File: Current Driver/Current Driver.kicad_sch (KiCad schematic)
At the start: 58 parts, among them J1 Conn_01x03, J2 Input, J3 Load, J4 VP BJT Conn, J5 VN BJT Conn, Q1 BC817, Q2 BC807, Q3 D45H11G, Q4 D44H11G, Q5 D45H11, Q6 D44H11G, U1 ADA4622-2xCP, U2 ADA4622-2xCP

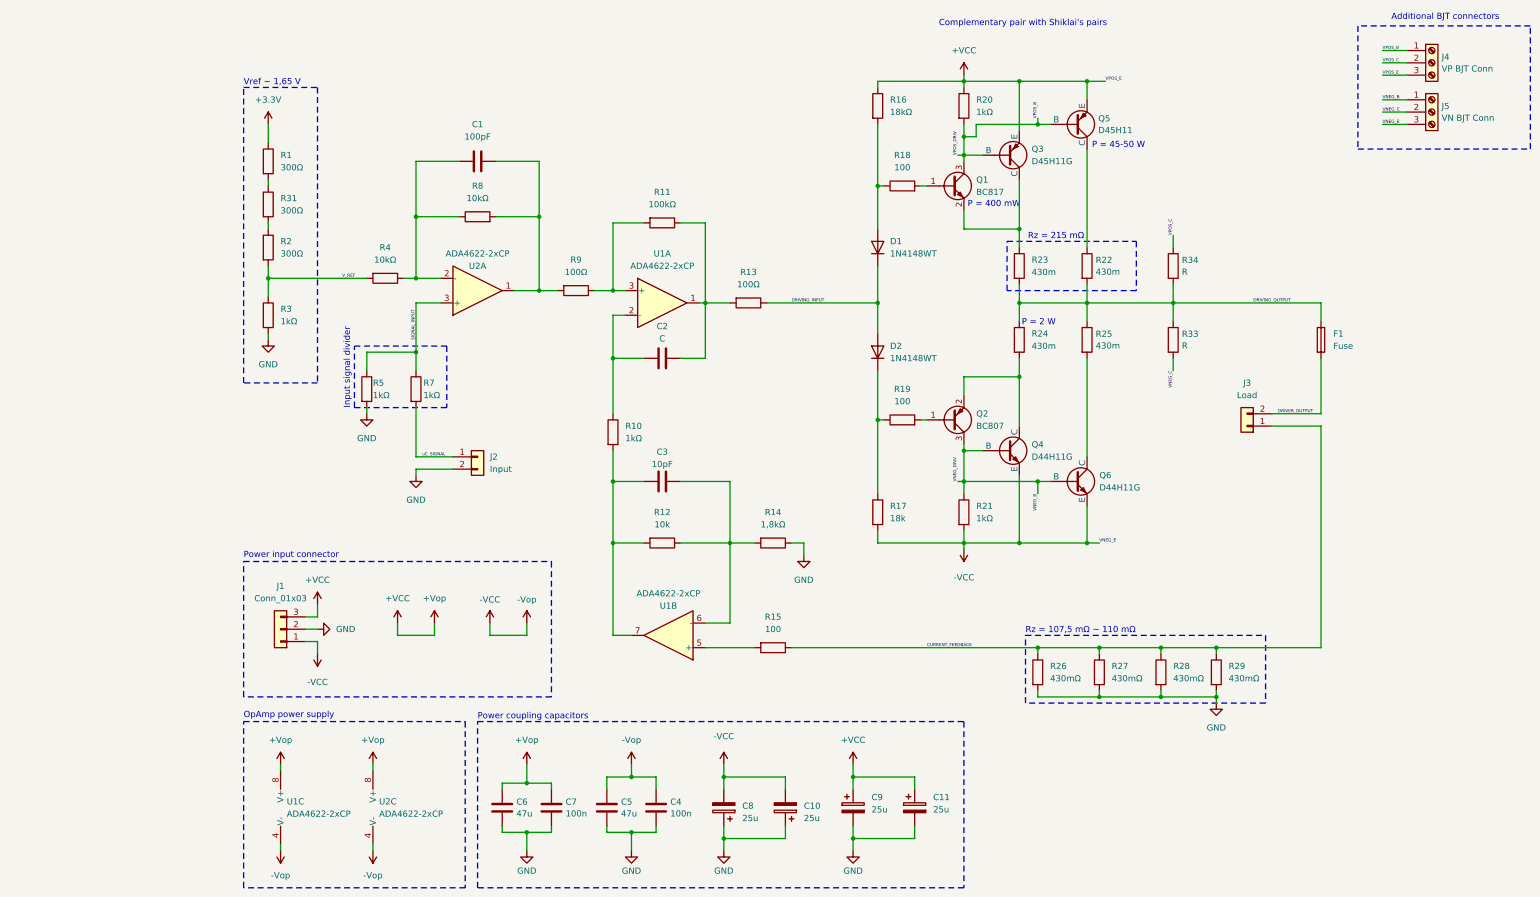
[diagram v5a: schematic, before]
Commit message: Edit Schematic
Added opAmp for stable reference voltage. Anotated schematic
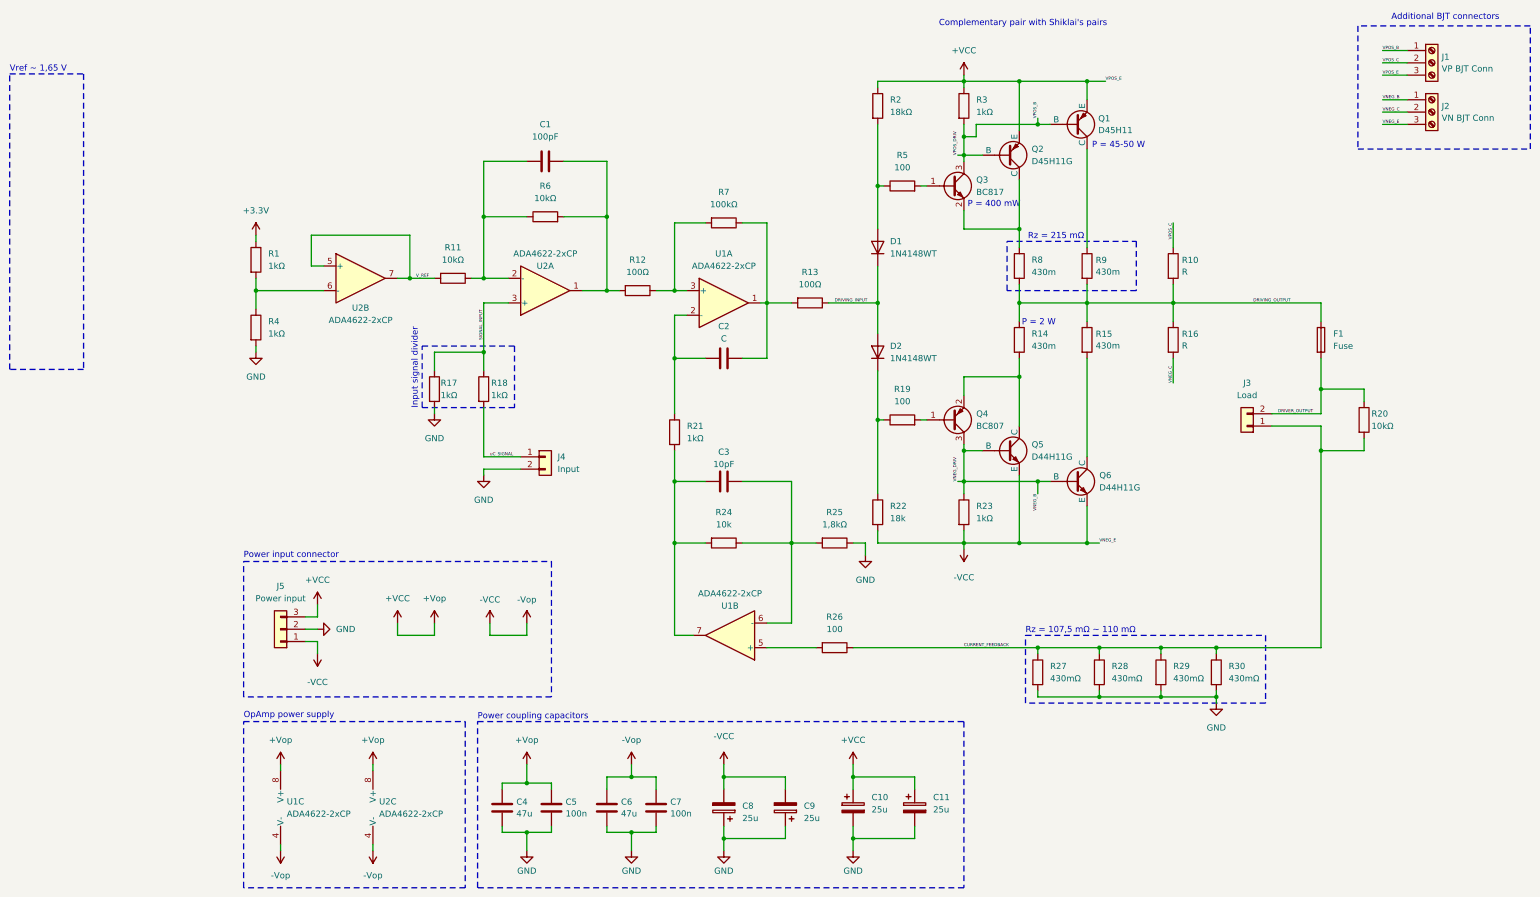
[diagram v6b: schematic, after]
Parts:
- removed R1, R31: 300Ω, Resistor_SMD:R_0805_2012Metric_Pad1.20x1.40mm_HandSolder, symbol Device:R
- added R20: 10kΩ, Resistor_SMD:R_0805_2012Metric_Pad1.20x1.40mm_HandSolder, symbol Device:R
- added unit 2 of U2
- J5: renamed from J1; value Conn_01x03 -> Power input
- R1: renamed from R2; value 300Ω -> 1kΩ
- renumbered C9 to C10, C6 to C4, C7 to C5, C5 to C6, C4 to C7, C10 to C9, J4 to J1, J5 to J2, J2 to J4, Q5 to Q1, Q3 to Q2, Q1 to Q3, Q2 to Q4, Q4 to Q5, R34 to R10, R4 to R11, R9 to R12, R24 to R14, R25 to R15, R33 to R16, R5 to R17, R7 to R18, R16 to R2, R10 to R21, R17 to R22, R21 to R23, R12 to R24, R14 to R25, R15 to R26, R26 to R27, R27 to R28, R28 to R29, R20 to R3, R29 to R30, R3 to R4, R18 to R5, R8 to R6, R11 to R7, R23 to R8, R22 to R9
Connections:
- net +3.3V: now also R1.1
- net CURRENT_FEEDBACK: now also R20.2
- net DRIVER_OUTPUT: now also R20.1
- net V_REF: now also U2.5 (+), U2.7; no longer R1.2, R4.1
- new net: R1.2, R4.1, U2.6 (-)
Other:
- moved on the sheet: C1, C2, C3, J4, R1, R11, R12, R13, R17, R18, R21, R24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

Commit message: schematic update
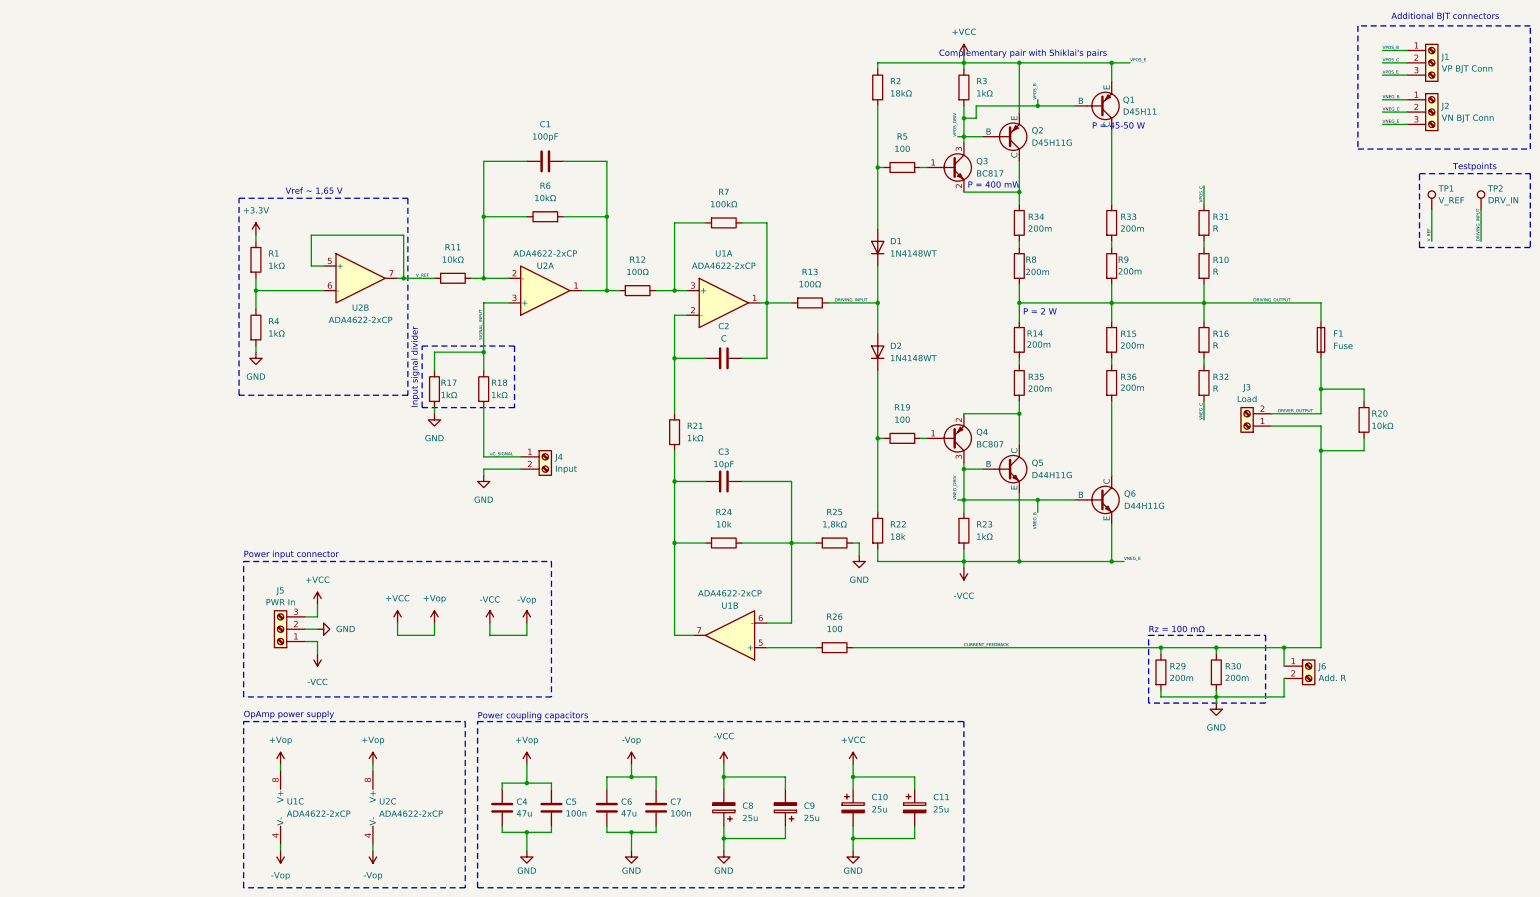
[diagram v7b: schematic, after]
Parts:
- removed J3: Load, symbol Connector_Generic:Conn_01x02
- removed J4: Input, symbol Connector_Generic:Conn_01x02
- removed J5: Power input, symbol Connector_Generic:Conn_01x03
- removed R27, R28: 430mΩ, Resistor_SMD:R_0805_2012Metric_Pad1.20x1.40mm_HandSolder, symbol Device:R
- added J3: Load, TerminalBlock:TerminalBlock_Xinya_XY308-2.54-2P_1x02_P2.54mm_Horizontal, symbol Connector:Screw_Terminal_01x02
- added J4: Input, TerminalBlock:TerminalBlock_Xinya_XY308-2.54-2P_1x02_P2.54mm_Horizontal, symbol Connector:Screw_Terminal_01x02
- added J5: PWR In, TerminalBlock:TerminalBlock_Xinya_XY308-2.54-3P_1x03_P2.54mm_Horizontal, symbol Connector:Screw_Terminal_01x03
- added J6: Add. R, TerminalBlock:TerminalBlock_Xinya_XY308-2.54-2P_1x02_P2.54mm_Horizontal, symbol Connector:Screw_Terminal_01x02
- added R31, R32: R, Resistor_SMD:R_2512_6332Metric_Pad1.40x3.35mm_HandSolder, symbol Device:R
- added R33, R34, R35, R36: 200m, Resistor_SMD:R_2512_6332Metric_Pad1.40x3.35mm_HandSolder, symbol Device:R
- added TP1: V_REF, TestPoint:TestPoint_Loop_D2.60mm_Drill1.4mm_Beaded, symbol Connector:TestPoint
- added TP2: DRV_IN, TestPoint:TestPoint_Loop_D2.60mm_Drill1.4mm_Beaded, symbol Connector:TestPoint
- Q1, Q2, Q6: footprint component_lib:TO254P1009X445X1985-3 -> component_lib:D44H11G
- Q5: footprint Package_TO_SOT_THT:TO-220-3_Vertical -> component_lib:D44H11G
- R10, R16: footprint Resistor_SMD:R_0805_2012Metric_Pad1.20x1.40mm_HandSolder -> Resistor_SMD:R_2512_6332Metric_Pad1.40x3.35mm_HandSolder
- R14, R15, R8, R9: value 430m -> 200m; footprint Resistor_SMD:R_0805_2012Metric_Pad1.20x1.40mm_HandSolder -> Resistor_SMD:R_2512_6332Metric_Pad1.40x3.35mm_HandSolder
- R29, R30: value 430mΩ -> 200m; footprint Resistor_SMD:R_0805_2012Metric_Pad1.20x1.40mm_HandSolder -> Resistor_SMD:R_2512_6332Metric_Pad1.40x3.35mm_HandSolder
- U1, U2: footprint Package_CSP:LFCSP-8-1EP_3x3mm_P0.5mm_EP1.45x1.74mm -> component_lib:ADA4522
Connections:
- net +VCC: now also J5.3 (Pin_3)
- net -VCC: now also J5.1 (Pin_1)
- net CURRENT_FEEDBACK: now also J3.1 (Pin_1), J6.1 (Pin_1)
- net DRIVER_OUTPUT: now also J3.2 (Pin_2)
- net DRIVING_INPUT: now also TP2.1
- net GND: now also J4.2 (Pin_2), J5.2 (Pin_2), J6.2 (Pin_2)
- net VNEG_C: now also R32.2; no longer R16.2
- net VPOS_C: now also R31.1; no longer R10.1
- net V_REF: now also TP1.1
- net uC_SIGNAL: now also J4.1 (Pin_1)
- net at Q4.2 (E), Q5.1 (C): now also R35.2; no longer R14.2
- net at R15.2: now also R36.1; no longer Q6.1 (C)
- net at Q2.1 (C), Q3.2 (E): now also R34.1; no longer R8.1
- net at Q1.1 (C): now also R33.1; no longer R9.1
- new net: R16.2, R32.1
- new net: R14.2, R35.1
- new net: R10.1, R31.2
- new net: R33.2, R9.1
- new net: Q6.1 (C), R36.2
- new net: R34.2, R8.1
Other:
- note added: "Rz = 100 mΩ"
- note added: "Testpoints"
- note removed: "Rz = 107,5 mΩ ~ 110 mΩ"
- note removed: "Rz = 215 mΩ"
- moved on the sheet: Q1, Q2, Q3, Q4, Q5, Q6, R10, R15, R16, R19, R2, R22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

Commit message: PCB_wersja1
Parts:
- removed J4: Input, TerminalBlock:TerminalBlock_Xinya_XY308-2.54-2P_1x02_P2.54mm_Horizontal, symbol Connector:Screw_Terminal_01x02
- added J4: Input, TerminalBlock:TerminalBlock_Xinya_XY308-2.54-3P_1x03_P2.54mm_Horizontal, symbol Connector:Screw_Terminal_01x03
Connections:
- net +3.3V: now also J4.3 (Pin_3)
- net GND: now also J4.2 (Pin_2)
- net uC_SIGNAL: now also J4.1 (Pin_1)
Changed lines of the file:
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@@
 	)
 	(symbol
+		(lib_id "power:+3.3V")
+		(at 73.66 111.76 180)
+		(unit 1)
+		(exclude_from_sim no)
+		(in_bom yes)
+		(on_board yes)
+		(dnp no)
+		(fields_autoplaced yes)
+		(property "Reference" "#PWR028"
+			(at 73.66 107.95 0)
+			(effects
+				(font
+					(size 1.27 1.27)
+				)
+				(hide yes)
+			)
+		)
+		(property "Value" "+3.3V"
+			(at 73.66 116.84 0)
+			(effects
+				(font
+					(size 1.27 1.27)
+				)
+			)
+		)
+		(property "Footprint" ""
+			(at 73.66 111.76 0)
+			(effects
+				(font
+					(size 1.27 1.27)
+				)
+				(hide yes)
+			)
+		)
+		(property "Datasheet" ""
+			(at 73.66 111.76 0)
+			(effects
+				(font
+					(size 1.27 1.27)
+				)
+				(hide yes)
+			)
+		)
+		(property "Description" "Power symbol creates a global label with name \"+3.3V\""
+			(at 73.66 111.76 0)
+			(effects
+				(font
+					(size 1.27 1.27)
+				)
+				(hide yes)
+			)
+		)
+		(pin "1"
+		)
+		(instances
+			(project "Current Driver"
+				(path "/0f8a692c-c9f3-4e4f-b21e-c051942eafa4"
+					(reference "#PWR028")
+					(unit 1)
+				)
+			)
+		)
+	)
+	(symbol
 		(lib_id "power:+1V0")
 		(at 43.18 187.96 180)
@@
 	)
 	(symbol
+		(lib_id "Connector:Screw_Terminal_01x03")
+		(at 78.74 109.22 0)
+		(unit 1)
+		(exclude_from_sim no)
+		(in_bom yes)
+		(on_board yes)
+		(dnp no)
+		(fields_autoplaced yes)
+		(property "Reference" "J4"
+			(at 81.28 107.9499 0)
+			(effects
+				(font
+					(size 1.27 1.27)
+				)
+				(justify left)
+			)
+		)
+		(property "Value" "Input"
+			(at 81.28 110.4899 0)
+			(effects
+				(font
+					(size 1.27 1.27)
+				)
+				(justify left)
+			)
+		)
+		(property "Footprint" "TerminalBlock:TerminalBlock_Xinya_XY308-2.54-3P_1x03_P2.54mm_Horizontal"
+			(at 78.74 109.22 0)
+			(effects
+				(font
+					(size 1.27 1.27)
+				)
+				(hide yes)
+			)
+		)
+		(property "Datasheet" "~"
+			(at 78.74 109.22 0)
+			(effects
+				(font
+					(size 1.27 1.27)
+				)
+				(hide yes)
+			)
+		)
+		(property "Description" "Generic screw terminal, single row, 01x03, script generated (kicad-library-utils/schlib/autogen/connector/)"
+			(at 78.74 109.22 0)
+			(effects
+				(font
+					(size 1.27 1.27)
+				)
+				(hide yes)
+			)
+		)
+		(pin "1"
+		)
+		(pin "2"
+		)
+		(pin "3"
+		)
+		(instances
+			(project "Current Driver"
+				(path "/0f8a692c-c9f3-4e4f-b21e-c051942eafa4"
+					(reference "J4")
+					(unit 1)
+				)
+			)
+		)
+	)
+	(symbol
 		(lib_id "power:GND")
 		(at 143.51 127 0)
@@
 					(unit 1)
 				)
-			)
-		)
-	)
-	(symbol
-		(lib_id "Connector:Screw_Terminal_01x02")
-		(at 78.74 106.68 0)
-		(unit 1)
-		(exclude_from_sim no)
-		(in_bom yes)
-		(on_board yes)
-		(dnp no)
-		(fields_autoplaced yes)
-		(property "Reference" "J4"
-			(at 80.772 106.7378 0)
-			(effects
-				(font
-					(size 1.27 1.27)
-				)
-				(justify left)
-			)
-		)
-		(property "Value" "Input"
-			(at 80.772 109.1621 0)
-			(effects
-				(font
-					(size 1.27 1.27)
-				)
-				(justify left)
-			)
-		)
-		(property "Footprint" "TerminalBlock:TerminalBlock_Xinya_XY308-2.54-2P_1x02_P2.54mm_Horizontal"
-			(at 78.74 106.68 0)
-			(effects
-				(font
-					(size 1.27 1.27)
-				)
-				(hide yes)
-			)
-		)
-		(property "Datasheet" "~"
-			(at 78.74 106.68 0)
-			(effects
-				(font
-					(size 1.27 1.27)
-				)
-				(hide yes)
-			)
-		)
-		(property "Description" "Generic screw terminal, single row, 01x02, script generated (kicad-library-utils/schlib/autogen/connector/)"
-			(at 78.74 106.68 0)
-			(effects
-				(font
-					(size 1.27 1.27)
-				)
-				(hide yes)
-			)
-		)
-		(pin "1"
-		)
-		(pin "2"
-		)
-		(instances
-			(project "Current Driver"
-				(path "/0f8a692c-c9f3-4e4f-b21e-c051942eafa4"
-					(reference "J4")
-					(unit 1)
-				)
